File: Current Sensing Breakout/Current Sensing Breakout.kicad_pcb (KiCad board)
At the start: 2 copper layers, 27.9 x 50.8 mm, 6 parts, among them U1 ACS725xLCTR-20AB

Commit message: Added silkscreen to board
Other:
- board text added: "Garrett McEntire Current Sensing Breakout"
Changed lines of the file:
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@@
     (effects (font (size 1 1) (thickness 0.15)) (justify left bottom))
+  )
+  (gr_text "Garrett McEntire\nCurrent Sensing\nBreakout" (at 74.676 66.294 90) (layer "F.SilkS")
+    (effects (font (size 1.5 1.5) (thickness 0.3) bold) (justify bottom))
   )
   (gr_text "MEAS" (at 66.294 58.928 90) (layer "F.SilkS")

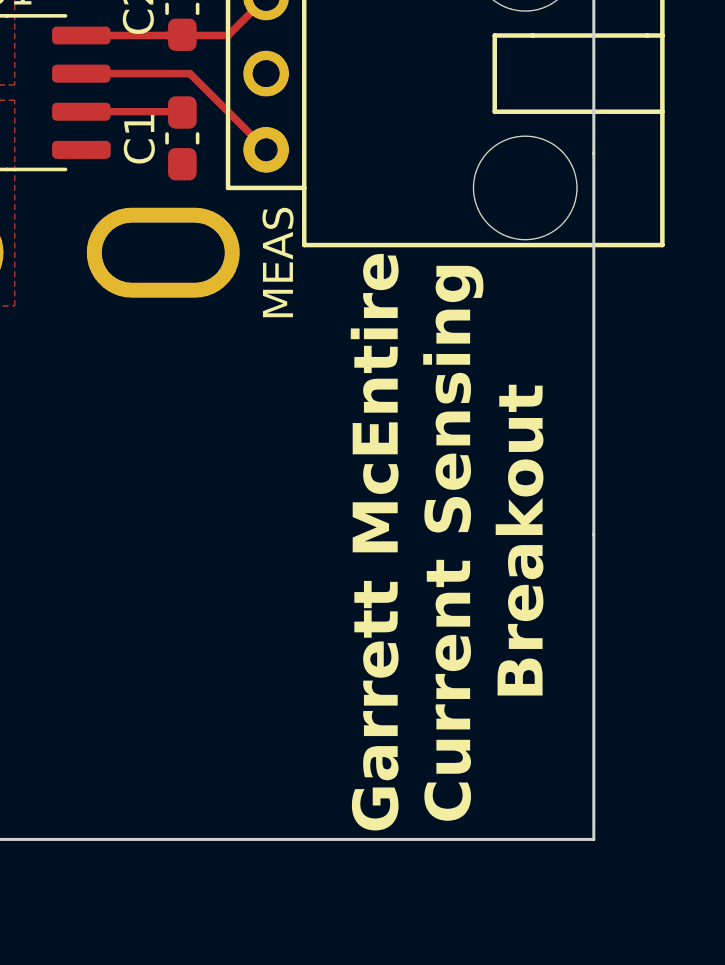
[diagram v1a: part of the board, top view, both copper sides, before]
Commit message: Fixed Silkscreen
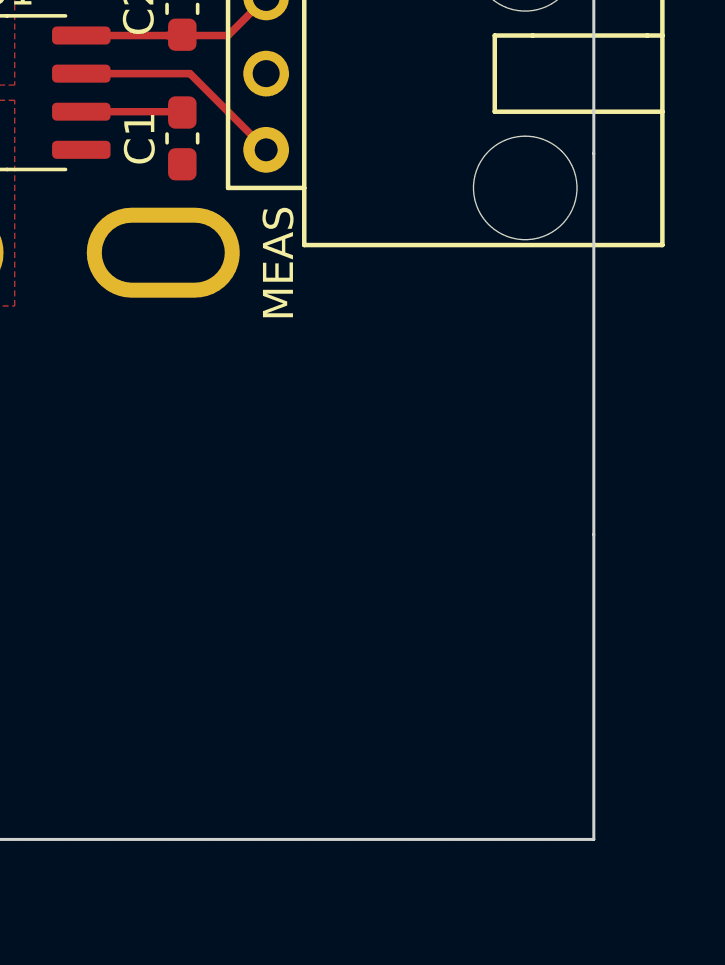
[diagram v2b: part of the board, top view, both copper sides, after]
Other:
- board text added: "Current Sensing Breakout Mars Rover Design Team Missouri S&T, 2024 Garrett McEntire"
- board text removed: "Garrett McEntire Current Sensing Breakout"
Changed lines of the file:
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@@
   (gr_line (start 76.2 76.2) (end 48.26 76.2)
     (stroke (width 0.1) (type default)) (layer "Edge.Cuts"))
+  (gr_text "Current Sensing Breakout\nMars Rover Design Team\nMissouri S&T, 2024\nGarrett McEntire" (at 75.438 33.274) (layer "B.SilkS")
+    (effects (font (size 1.143 1.143) (thickness 0.1875)) (justify left bottom mirror))
+  )
   (gr_text "3V3" (at 66.294 46.482 90) (layer "F.SilkS")
     (effects (font (size 1 1) (thickness 0.15)) (justify left bottom))
@@
     (effects (font (size 1 1) (thickness 0.15)) (justify left bottom))
   )
-  (gr_text "Garrett McEntire\nCurrent Sensing\nBreakout" (at 74.676 66.294 90) (layer "F.SilkS")
-    (effects (font (size 1.5 1.5) (thickness 0.3) bold) (justify bottom))
-  )
   (gr_text "MEAS" (at 66.294 58.928 90) (layer "F.SilkS")
